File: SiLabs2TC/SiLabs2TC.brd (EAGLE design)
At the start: 39.4 x 34 mm, 13 parts, among them U1 NCP1117LPST33T3G

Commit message: Major revamp of repo.
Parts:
- turned U1 to 180 degrees
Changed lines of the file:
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@@
 <?xml version="1.0" encoding="utf-8"?>
 <!DOCTYPE eagle SYSTEM "eagle.dtd">
-<eagle version="7.6.0">
+<eagle version="7.4.0">
 <drawing>
 <settings>
@@
 <attribute name="HOUSEPART" value="YES" x="2.921" y="28.575" size="1.778" layer="27" rot="R270" display="off"/>
 </element>
-<element name="U1" library="MF_IC_Power" package="SOT-223-3" value="NCP1117LPST33T3G" x="28.575" y="28.575" smashed="yes" rot="R90">
-<attribute name="NAME" x="24.075" y="25.325" size="1.27" layer="25" font="vector" ratio="16" rot="R90"/>
-<attribute name="URL" value="http://www.onsemi.com/pub_link/Collateral/NCP1117LP-D.PDF" x="28.575" y="28.575" size="1.778" layer="27" rot="R90" display="off"/>
-<attribute name="VALUE" value="NCP1117LPST33T3G" x="28.575" y="28.575" size="1.778" layer="27" rot="R90" display="off"/>
-<attribute name="POPULATE" value="1" x="28.575" y="28.575" size="1.778" layer="27" rot="R90" display="off"/>
-<attribute name="MPN" value="NCP1117LPST33T3G" x="28.575" y="28.575" size="1.778" layer="27" rot="R90" display="off"/>
-<attribute name="HOUSEPART" value="NO" x="28.575" y="28.575" size="1.778" layer="27" rot="R90" display="off"/>
+<element name="U1" library="MF_IC_Power" package="SOT-223-3" value="NCP1117LPST33T3G" x="28.575" y="28.575" smashed="yes" rot="R180">
+<attribute name="NAME" x="22.661" y="28.523" size="1.27" layer="25" font="vector" ratio="16" rot="R270"/>
+<attribute name="URL" value="http://www.onsemi.com/pub_link/Collateral/NCP1117LP-D.PDF" x="28.575" y="28.575" size="1.778" layer="27" rot="R180" display="off"/>
+<attribute name="VALUE" value="NCP1117LPST33T3G" x="28.575" y="28.575" size="1.778" layer="27" rot="R180" display="off"/>
+<attribute name="POPULATE" value="1" x="28.575" y="28.575" size="1.778" layer="27" rot="R180" display="off"/>
+<attribute name="MPN" value="NCP1117LPST33T3G" x="28.575" y="28.575" size="1.778" layer="27" rot="R180" display="off"/>
+<attribute name="HOUSEPART" value="NO" x="28.575" y="28.575" size="1.778" layer="27" rot="R180" display="off"/>
 </element>
 <element name="F1" library="PP_Passives" package="1206" value="0ZCJ0010FF2E" x="9.525" y="30.353" rot="R90">
@@
 <attribute name="HOUSEPART" value="" x="36.195" y="26.67" size="1.778" layer="27" rot="R180" display="off"/>
 </element>
-<element name="U$3" library="PP_Aesthetics" package="MF_LOGO_MEDIUM" value="MF_LOGOLOGO_MEDIUM" x="28.194" y="7.112" rot="R90"/>
+<element name="U$3" library="PP_Aesthetics" package="MF_LOGO_MEDIUM" value="MF_LOGOLOGO_MEDIUM" x="28.194" y="7.112" rot="R90">
+<attribute name="POPULATE" value="0" x="28.194" y="7.112" size="1.778" layer="27" rot="R90" display="off"/>
+<attribute name="MPN" value="" x="28.194" y="7.112" size="1.778" layer="27" rot="R90" display="off"/>
+</element>
 <element name="SI_PROGRAMMER" library="PP_Connectors" package="5103308-1" value="5103308-1" x="5.588" y="10.922" rot="R90">
 <attribute name="LABEL03" value="GND" x="5.588" y="10.922" size="1.778" layer="27" rot="R90" display="off"/>
@@
 <attribute name="POPULATE" value="1" x="5.588" y="10.922" size="1.778" layer="27" rot="R90" display="off"/>
 <attribute name="MPN" value="5103308-1" x="5.588" y="10.922" size="1.778" layer="27" rot="R90" display="off"/>
+<attribute name="HOUSEPART" value="" x="5.588" y="10.922" size="1.778" layer="27" rot="R90" display="off"/>
+<attribute name="VALUE" value="5103308-1" x="5.588" y="10.922" size="1.778" layer="27" rot="R90" display="off"/>
+<attribute name="URL" value="" x="5.588" y="10.922" size="1.778" layer="27" rot="R90" display="off"/>
 </element>
 <element name="TC2030" library="PP_Connectors" package="30306-6002HB" value="30306-6002HB" x="34.036" y="10.922" rot="R270">
 <attribute name="POPULATE" value="1" x="34.036" y="10.922" size="1.778" layer="27" rot="R270" display="off"/>
-<attribute name="LABEL02" value="VCC" x="34.036" y="10.922" size="1.778" layer="27" rot="R270" display="off"/>
-<attribute name="LABEL01" value="GND" x="34.036" y="10.922" size="1.778" layer="27" rot="R270" display="off"/>
-<attribute name="LABEL04" value="C2D" x="34.036" y="10.922" size="1.778" layer="27" rot="R270" display="off"/>
-<attribute name="LABEL03" value="!RST!/C2CK" x="34.036" y="10.922" size="1.778" layer="27" rot="R270" display="off"/>
+<attribute name="LABEL02" value="" x="34.036" y="10.922" size="1.778" layer="27" rot="R270" display="off"/>
+<attribute name="LABEL01" value="" x="34.036" y="10.922" size="1.778" layer="27" rot="R270" display="off"/>
+<attribute name="LABEL04" value="" x="34.036" y="10.922" size="1.778" layer="27" rot="R270" display="off"/>
+<attribute name="LABEL03" value="" x="34.036" y="10.922" size="1.778" layer="27" rot="R270" display="off"/>
 <attribute name="LABEL05" value="" x="34.036" y="10.922" size="1.778" layer="27" rot="R270" display="off"/>
 <attribute name="LABEL06" value="" x="34.036" y="10.922" size="1.778" layer="27" rot="R270" display="off"/>
 <attribute name="MPN" value="30306-6002HB" x="34.036" y="10.922" size="1.778" layer="27" rot="R270" display="off"/>
+<attribute name="HOUSEPART" value="" x="34.036" y="10.922" size="1.778" layer="27" rot="R270" display="off"/>
+<attribute name="VALUE" value="30306-6002HB" x="34.036" y="10.922" size="1.778" layer="27" rot="R270" display="off"/>
+<attribute name="URL" value="" x="34.036" y="10.922" size="1.778" layer="27" rot="R270" display="off"/>
 </element>
 <element name="C1" library="MF_Passives" package="C1206" value="10uF" x="15.24" y="27.305" smashed="yes" rot="R180">
@@
 <wire x1="33.909" y1="28.575" x2="34.945" y2="29.611" width="0.254" layer="1"/>
 <wire x1="34.945" y1="29.611" x2="34.945" y2="30.48" width="0.254" layer="1"/>
-<wire x1="25.325" y1="28.575" x2="27.175" y2="28.575" width="0.4064" layer="1"/>
-<wire x1="31.825" y1="28.575" x2="27.175" y2="28.575" width="0.4064" layer="1"/>
+<wire x1="31.825" y1="28.575" x2="25.325" y2="28.575" width="0.4064" layer="1"/>
 <contactref element="TC2030" pad="2"/>
 <wire x1="27.175" y1="19.561" x2="30.226" y2="16.51" width="0.4064" layer="1"/>

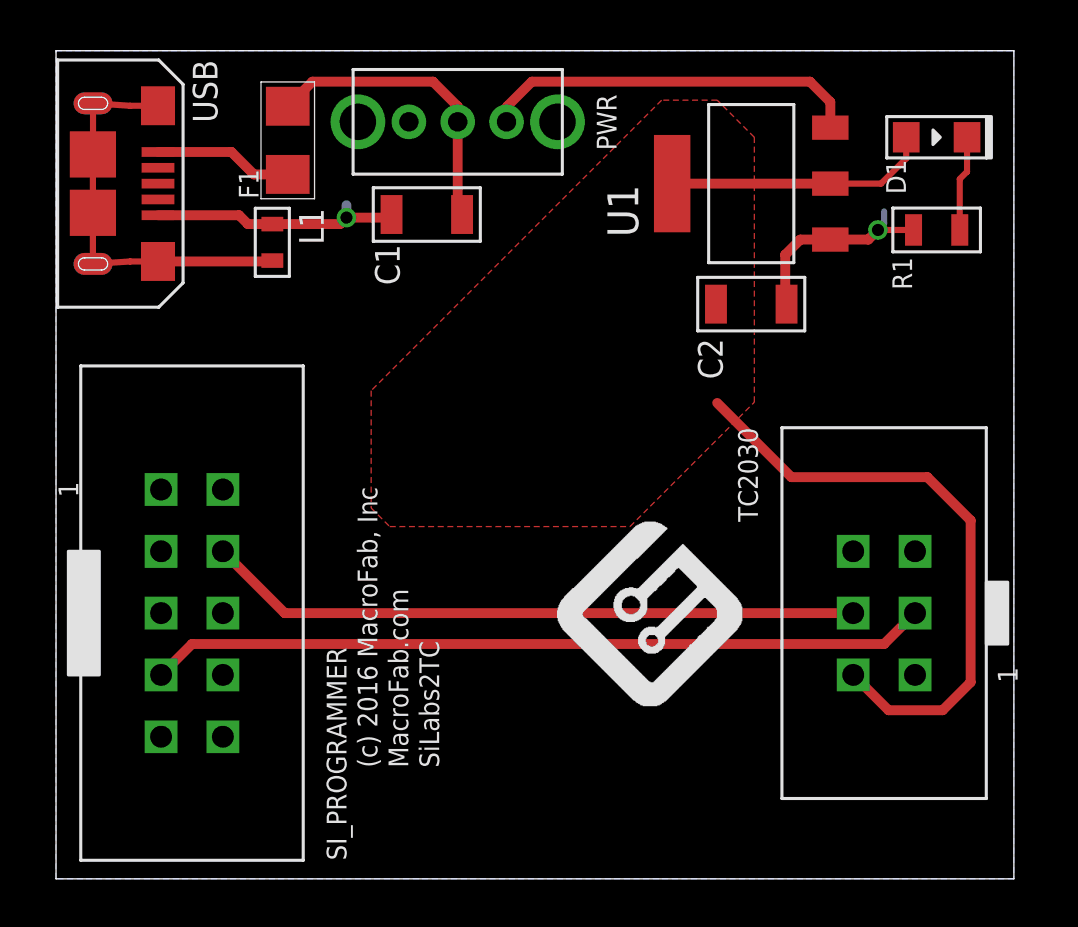
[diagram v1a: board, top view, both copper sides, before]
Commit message: Added Pin sharing support for TagConnect.
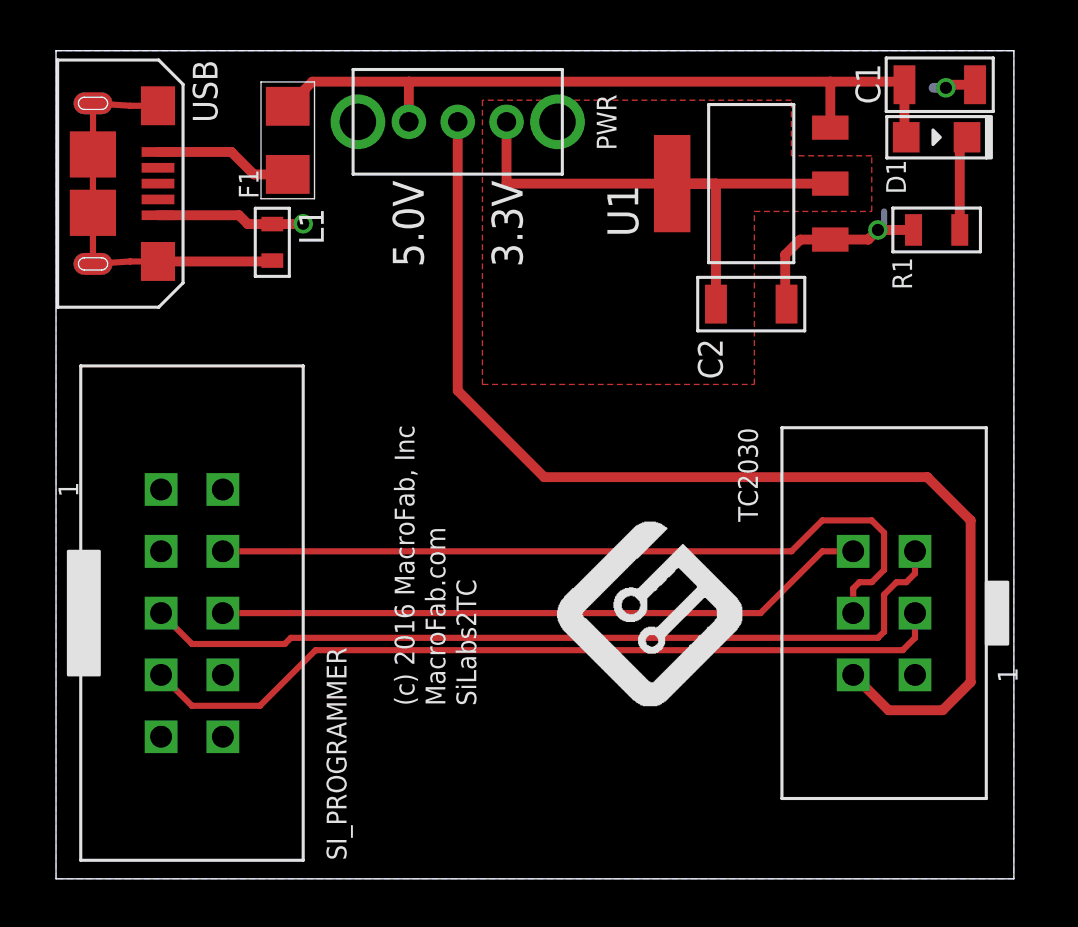
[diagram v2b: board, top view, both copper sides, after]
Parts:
- moved C1 21.7 mm to (36.3, 32.6), turned to 0 degrees
- moved FRAME1 2.96 mm to (13.5, 7.11)
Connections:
- removed net N$2: C1.P$1, F1.2, PWR.2
- removed net N$5: PWR.1, U1.P$4
- new net 3.3V: C2.P$1, PWR.1, U1.P$1, U1.P$3
- new net C2CK_PS: SI_PROGRAMMER.5, TC2030.5
- new net C2D_PS: SI_PROGRAMMER.6, TC2030.6
- new net USB_5VF: C1.P$1, D1.ANODE, F1.2, PWR.3, U1.P$4
- net VCC: now also PWR.2; no longer C2.P$1, D1.ANODE, U1.P$1, U1.P$3
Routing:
- net C2CK_PS: track 0.00 -> 34.5 mm
- net USB_5VF: track 0.00 -> 31.6 mm
- net C2D_PS: track 0.00 -> 27.0 mm
- net 3.3V: track 0.00 -> 22.6 mm
- net N$5: track 15.8 -> 0.00 mm
- net N$2: track 12.5 -> 0.00 mm
- net VCC: track 35.9 -> 46.9 mm
- net C2D: track 27.0 -> 32.0 mm
- net GND: track 19.2 -> 16.5 mm, vias 2 -> 3
- net !RST!/C2CK: track 32.0 -> 33.7 mm
- added copper zone on layer 1, net 3.3V
- removed copper zone on layer 1, net VCC
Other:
- board text added: "3.3V"
- board text added: "5.0V"
